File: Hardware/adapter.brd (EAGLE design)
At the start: 61.9 x 62.5 mm, 7 parts

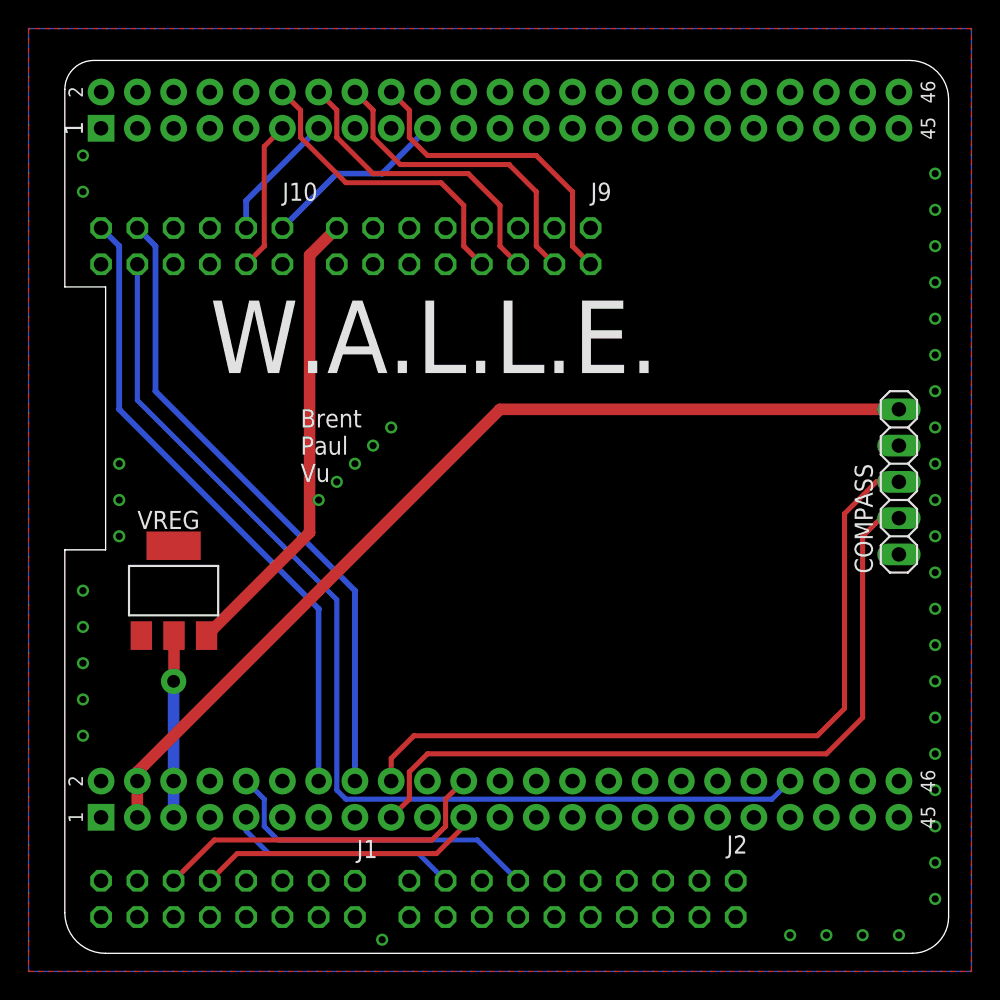
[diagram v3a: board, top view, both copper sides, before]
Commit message: Update schematic to be sectioned off and organized.
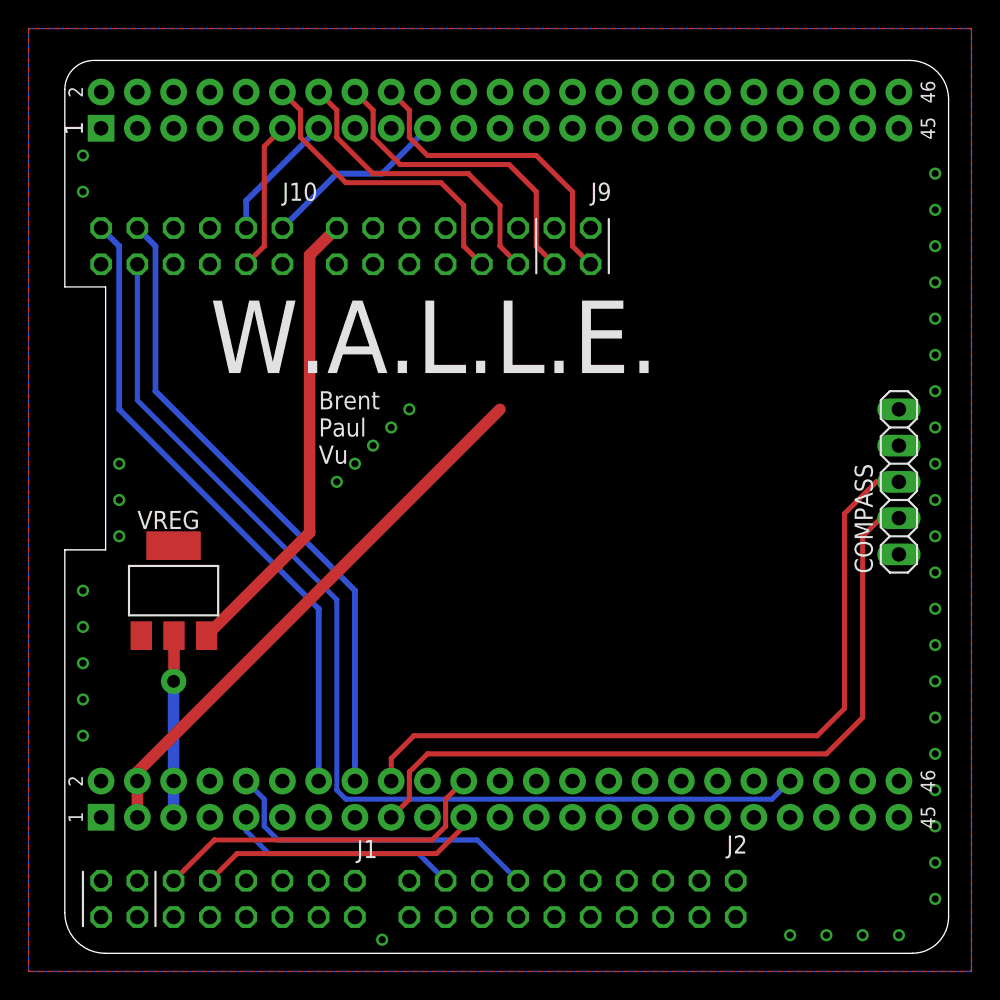
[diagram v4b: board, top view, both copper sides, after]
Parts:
- COMPASS: value (none) -> HMC5883L
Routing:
- net 3.3V: track 67.0 -> 39.1 mm
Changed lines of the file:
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@@
 <layer number="37" name="tTest" color="7" fill="1" visible="no" active="yes"/>
 <layer number="38" name="bTest" color="7" fill="1" visible="no" active="yes"/>
-<layer number="39" name="tKeepout" color="4" fill="11" visible="yes" active="yes"/>
-<layer number="40" name="bKeepout" color="1" fill="11" visible="yes" active="yes"/>
-<layer number="41" name="tRestrict" color="4" fill="10" visible="yes" active="yes"/>
-<layer number="42" name="bRestrict" color="1" fill="10" visible="yes" active="yes"/>
-<layer number="43" name="vRestrict" color="2" fill="10" visible="yes" active="yes"/>
+<layer number="39" name="tKeepout" color="4" fill="11" visible="no" active="yes"/>
+<layer number="40" name="bKeepout" color="1" fill="11" visible="no" active="yes"/>
+<layer number="41" name="tRestrict" color="4" fill="10" visible="no" active="yes"/>
+<layer number="42" name="bRestrict" color="1" fill="10" visible="no" active="yes"/>
+<layer number="43" name="vRestrict" color="2" fill="10" visible="no" active="yes"/>
 <layer number="44" name="Drills" color="7" fill="1" visible="no" active="yes"/>
 <layer number="45" name="Holes" color="7" fill="1" visible="no" active="yes"/>
@@
 <layer number="50" name="dxf" color="7" fill="1" visible="no" active="no"/>
 <layer number="51" name="tDocu" color="7" fill="1" visible="yes" active="yes"/>
-<layer number="52" name="bDocu" color="7" fill="1" visible="yes" active="yes"/>
+<layer number="52" name="bDocu" color="7" fill="1" visible="no" active="yes"/>
 <layer number="53" name="tGND_GNDA" color="7" fill="9" visible="no" active="no"/>
 <layer number="54" name="bGND_GNDA" color="1" fill="9" visible="no" active="no"/>
@@
 <layer number="98" name="Guide" color="6" fill="1" visible="no" active="no"/>
 <layer number="100" name="Muster" color="7" fill="1" visible="no" active="no"/>
-<layer number="101" name="Patch_Top" color="12" fill="4" visible="yes" active="yes"/>
-<layer number="102" name="Vscore" color="7" fill="1" visible="yes" active="yes"/>
-<layer number="103" name="tMap" color="7" fill="1" visible="yes" active="yes"/>
-<layer number="104" name="Name" color="16" fill="1" visible="yes" active="yes"/>
-<layer number="105" name="tPlate" color="7" fill="1" visible="yes" active="yes"/>
-<layer number="106" name="bPlate" color="7" fill="1" visible="yes" active="yes"/>
-<layer number="107" name="Crop" color="7" fill="1" visible="yes" active="yes"/>
-<layer number="116" name="Patch_BOT" color="9" fill="4" visible="yes" active="yes"/>
-<layer number="121" name="_tsilk" color="7" fill="1" visible="yes" active="yes"/>
-<layer number="122" name="_bsilk" color="7" fill="1" visible="yes" active="yes"/>
-<layer number="125" name="_tNames" color="7" fill="1" visible="yes" active="yes"/>
-<layer number="144" name="Drill_legend" color="7" fill="1" visible="yes" active="yes"/>
-<layer number="151" name="HeatSink" color="7" fill="1" visible="yes" active="yes"/>
-<layer number="200" name="200bmp" color="1" fill="10" visible="yes" active="yes"/>
-<layer number="201" name="201bmp" color="2" fill="10" visible="yes" active="yes"/>
-<layer number="202" name="202bmp" color="3" fill="10" visible="yes" active="yes"/>
-<layer number="203" name="203bmp" color="4" fill="10" visible="yes" active="yes"/>
-<layer number="204" name="204bmp" color="5" fill="10" visible="yes" active="yes"/>
-<layer number="205" name="205bmp" color="6" fill="10" visible="yes" active="yes"/>
-<layer number="206" name="206bmp" color="7" fill="10" visible="yes" active="yes"/>
-<layer number="207" name="207bmp" color="8" fill="10" visible="yes" active="yes"/>
-<layer number="208" name="208bmp" color="9" fill="10" visible="yes" active="yes"/>
-<layer number="209" name="209bmp" color="7" fill="1" visible="yes" active="yes"/>
-<layer number="210" name="210bmp" color="7" fill="1" visible="yes" active="yes"/>
-<layer number="211" name="211bmp" color="7" fill="1" visible="yes" active="yes"/>
-<layer number="212" name="212bmp" color="7" fill="1" visible="yes" active="yes"/>
-<layer number="213" name="213bmp" color="7" fill="1" visible="yes" active="yes"/>
-<layer number="214" name="214bmp" color="7" fill="1" visible="yes" active="yes"/>
-<layer number="215" name="215bmp" color="7" fill="1" visible="yes" active="yes"/>
-<layer number="216" name="216bmp" color="7" fill="1" visible="yes" active="yes"/>
+<layer number="101" name="Patch_Top" color="12" fill="4" visible="no" active="yes"/>
+<layer number="102" name="Vscore" color="7" fill="1" visible="no" active="yes"/>
+<layer number="103" name="tMap" color="7" fill="1" visible="no" active="yes"/>
+<layer number="104" name="Name" color="16" fill="1" visible="no" active="yes"/>
+<layer number="105" name="tPlate" color="7" fill="1" visible="no" active="yes"/>
+<layer number="106" name="bPlate" color="7" fill="1" visible="no" active="yes"/>
+<layer number="107" name="Crop" color="7" fill="1" visible="no" active="yes"/>
+<layer number="108" name="tplace-old" color="10" fill="1" visible="no" active="yes"/>
+<layer number="109" name="ref-old" color="11" fill="1" visible="no" active="yes"/>
+<layer number="116" name="Patch_BOT" color="9" fill="4" visible="no" active="yes"/>
+<layer number="121" name="_tsilk" color="7" fill="1" visible="no" active="yes"/>
+<layer number="122" name="_bsilk" color="7" fill="1" visible="no" active="yes"/>
+<layer number="125" name="_tNames" color="7" fill="1" visible="no" active="yes"/>
+<layer number="144" name="Drill_legend" color="7" fill="1" visible="no" active="yes"/>
+<layer number="151" name="HeatSink" color="7" fill="1" visible="no" active="yes"/>
+<layer number="199" name="Contour" color="7" fill="1" visible="yes" active="yes"/>
+<layer number="200" name="200bmp" color="1" fill="10" visible="no" active="yes"/>
+<layer number="201" name="201bmp" color="2" fill="10" visible="no" active="yes"/>
+<layer number="202" name="202bmp" color="3" fill="10" visible="no" active="yes"/>
+<layer number="203" name="203bmp" color="4" fill="10" visible="no" active="yes"/>
+<layer number="204" name="204bmp" color="5" fill="10" visible="no" active="yes"/>
+<layer number="205" name="205bmp" color="6" fill="10" visible="no" active="yes"/>
+<layer number="206" name="206bmp" color="7" fill="10" visible="no" active="yes"/>
+<layer number="207" name="207bmp" color="8" fill="10" visible="no" active="yes"/>
+<layer number="208" name="208bmp" color="9" fill="10" visible="no" active="yes"/>
+<layer number="209" name="209bmp" color="7" fill="1" visible="no" active="yes"/>
+<layer number="210" name="210bmp" color="7" fill="1" visible="no" active="yes"/>
+<layer number="211" name="211bmp" color="7" fill="1" visible="no" active="yes"/>
+<layer number="212" name="212bmp" color="7" fill="1" visible="no" active="yes"/>
+<layer number="213" name="213bmp" color="7" fill="1" visible="no" active="yes"/>
+<layer number="214" name="214bmp" color="7" fill="1" visible="no" active="yes"/>
+<layer number="215" name="215bmp" color="7" fill="1" visible="no" active="yes"/>
+<layer number="216" name="216bmp" color="7" fill="1" visible="no" active="yes"/>
 <layer number="217" name="217bmp" color="18" fill="1" visible="no" active="no"/>
 <layer number="218" name="218bmp" color="19" fill="1" visible="no" active="no"/>
@@
 <layer number="250" name="Descript" color="3" fill="1" visible="no" active="no"/>
 <layer number="251" name="SMDround" color="12" fill="11" visible="no" active="no"/>
-<layer number="254" name="cooling" color="7" fill="1" visible="yes" active="yes"/>
+<layer number="254" name="cooling" color="7" fill="1" visible="no" active="yes"/>
 </layers>
 <board>
@@
 <wire x1="29.5275" y1="29.5275" x2="26.67" y2="29.5275" width="0" layer="20"/>
 <text x="36.83" y="41.91" size="5.08" layer="21">W.A.L.L.E.</text>
-<text x="43.18" y="34.29" size="1.27" layer="21">Brent
+<text x="44.45" y="35.56" size="1.27" layer="21">Brent
 Paul
 Vu</text>
@@
 </autorouter>
 <elements>
-<element name="COMPASS" library="pinhead" package="1X05" value="" x="85.09" y="34.29" rot="R90"/>
+<element name="COMPASS" library="pinhead" package="1X05" value="HMC5883L" x="85.09" y="34.29" rot="R90"/>
 <element name="J10" library="pinhead" package="2X06" value="" x="35.56" y="50.8" smashed="yes" rot="MR0">
 <attribute name="NAME" x="41.91" y="53.975" size="1.27" layer="25" ratio="10"/>
@@
 <via x="27.94" y="54.61" extent="1-16" drill="0.5"/>
 <via x="27.94" y="57.15" extent="1-16" drill="0.5"/>
-<via x="44.45" y="33.02" extent="1-16" drill="0.5"/>
+<via x="50.8" y="39.37" extent="1-16" drill="0.5"/>
 <via x="45.72" y="34.29" extent="1-16" drill="0.5"/>
 <via x="46.99" y="35.56" extent="1-16" drill="0.5"/>
@@
 </signal>
 <signal name="3.3V">
-<contactref element="COMPASS" pad="5"/>
 <contactref element="U$1" pad="P9.3"/>
 <contactref element="U$1" pad="P9.4"/>
@@
 <wire x1="31.75" y1="13.335" x2="31.75" y2="13.97" width="0.8128" layer="1"/>
 <wire x1="31.75" y1="13.97" x2="57.15" y2="39.37" width="0.8128" layer="1"/>
-<wire x1="57.15" y1="39.37" x2="85.09" y2="39.37" width="0.8128" layer="1"/>
+<contactref element="COMPASS" pad="5"/>
+<wire x1="57.15" y1="39.37" x2="85.09" y2="39.37" width="0" layer="19" extent="1-1"/>
 </signal>
 <signal name="PWM1A">

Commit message: Updated header dimensions. Added Extra connector for GPIO.
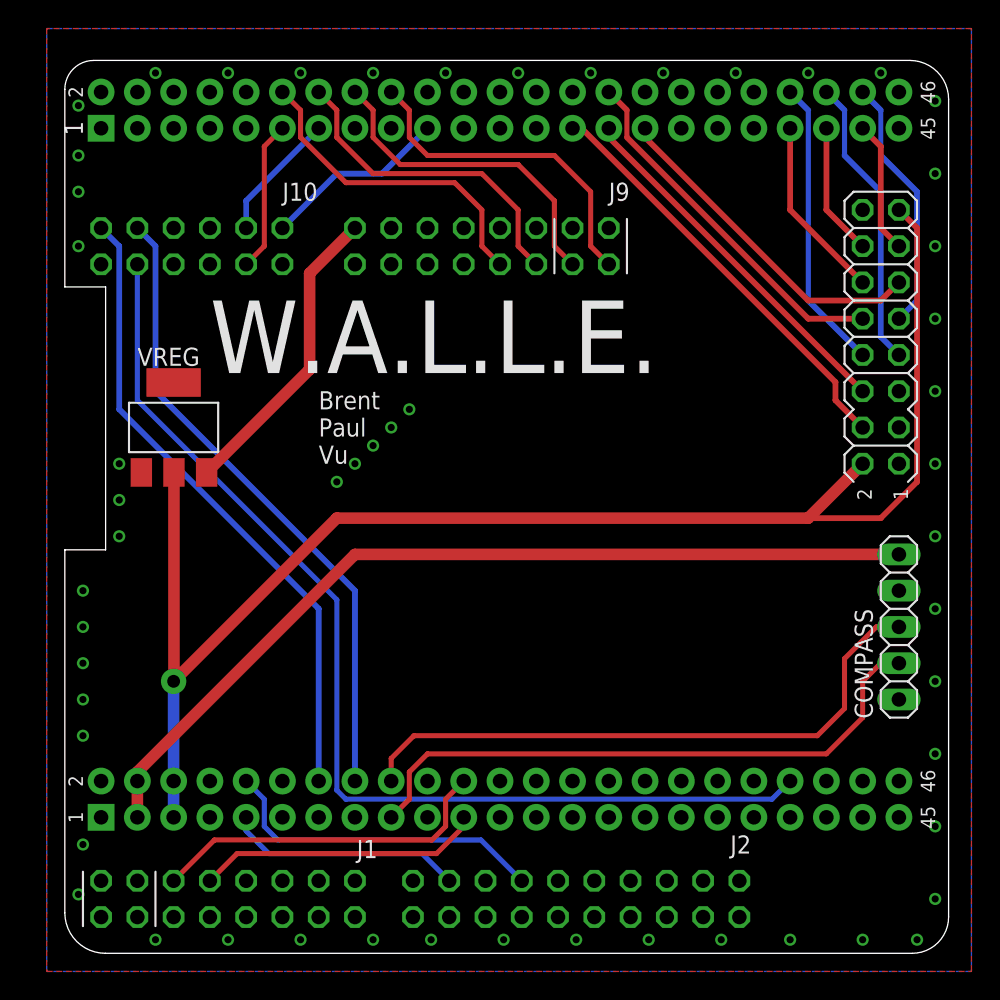
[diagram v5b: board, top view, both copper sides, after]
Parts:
- added EXTRA: EXT, pinhead:2X08
- moved VREG 11.4 mm to (34.3, 38.1)
- moved COMPASS 10.2 mm to (85.1, 24.1)
- moved J9 1.27 mm to (55.9, 50.8)
- moved J2 0.25 mm to (62.5, 5.08)
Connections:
- new net EX1: EXTRA.4, U$1.P8.27
- new net EX10: EXTRA.10, U$1.P8.30
- new net EX2: EXTRA.6, U$1.P8.29
- new net EX3: EXTRA.11, U$1.P8.31
- new net EX4: EXTRA.12, U$1.P8.39
- new net EX5: EXTRA.14, U$1.P8.41
- new net EX6: EXTRA.13, U$1.P8.43
- new net EX7: EXTRA.8, U$1.P8.40
- new net EX8: EXTRA.7, U$1.P8.42
- new net EX9: EXTRA.9, U$1.P8.44
- new net N$7: EXTRA.3
- net 5V: now also EXTRA.15, EXTRA.2
- net GND: now also EXTRA.1, EXTRA.16, EXTRA.5
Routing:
- net 5V: track 12.7 -> 121.6 mm
- net EX1: track 0.00 -> 29.7 mm
- net EX2: track 0.00 -> 25.8 mm
- net EX10: track 0.00 -> 25.5 mm
- net 3.3V: track 39.1 -> 62.8 mm
- net EX3: track 0.00 -> 23.7 mm
- net EX8: track 0.00 -> 20.5 mm
- net EX7: track 0.00 -> 20.5 mm
- net EX9: track 0.00 -> 18.0 mm
- net EX4: track 0.00 -> 12.9 mm
- net VBAT: track 32.3 -> 21.4 mm
- net I2C1_SDA: track 53.2 -> 43.0 mm
- net I2C1_SCL: track 52.8 -> 42.6 mm
- net EX6: track 0.00 -> 9.31 mm
- net EX5: track 0.00 -> 9.31 mm
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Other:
- board text added: "1"
- board text added: "2"
